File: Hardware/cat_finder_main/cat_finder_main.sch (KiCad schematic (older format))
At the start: 28 parts, among them J1 BATT, J10 Analog, J2 BME280, J3 CSS811, J4 DRIVERS, J5 GY-87, J7 FTDI, J8 Digital, J9 i2c, SW1 SW_DIP_x02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

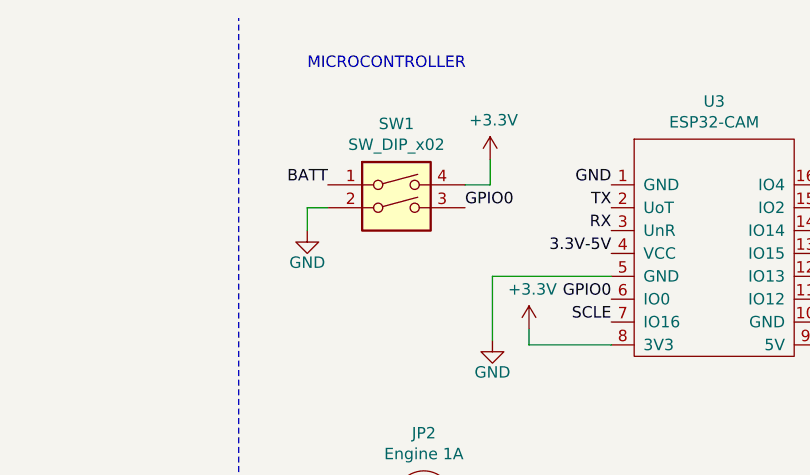
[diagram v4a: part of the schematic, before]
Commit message: change prog pines delete switch
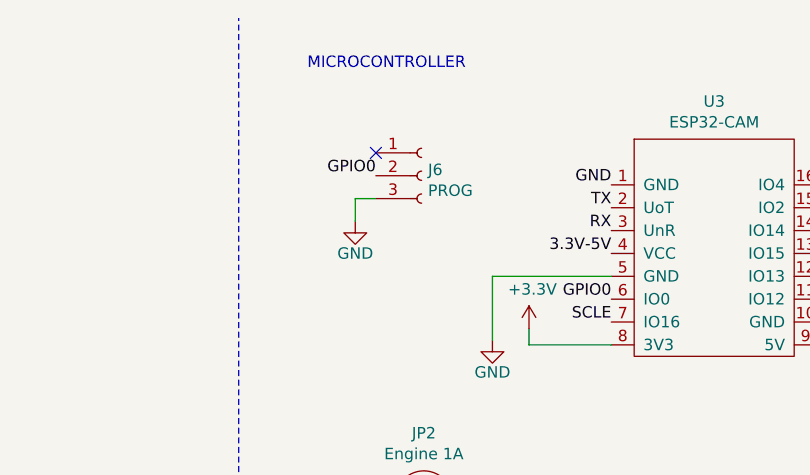
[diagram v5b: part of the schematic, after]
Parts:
- removed SW1: SW_DIP_x02, connectors:DP-02, symbol Switch:SW_DIP_x02
- added J6: PROG, Connector_PinHeader_2.54mm:PinHeader_1x03_P2.54mm_Vertical, symbol Connector:Conn_01x03_Female
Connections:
- net GND: now also J6.3 (Pin_3)
- net GPIO0: now also J6.2 (Pin_2)
- no-connect marks 4 -> 5
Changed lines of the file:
@@
 L power:GND #PWR023
 U 1 1 5D494473
-P 7300 1400
-F 0 "#PWR023" H 7300 1150 50  0001 C CNN
-F 1 "GND" H 7300 1260 50  0000 C CNN
-F 2 "" H 7300 1400 50  0001 C CNN
-F 3 "" H 7300 1400 50  0001 C CNN
-	1    7300 1400
-	1    0    0    -1
-$EndComp
-Text Label 7990 1300 0    50   ~ 0
+P 7510 1360
+F 0 "#PWR023" H 7510 1110 50  0001 C CNN
+F 1 "GND" H 7510 1220 50  0000 C CNN
+F 2 "" H 7510 1360 50  0001 C CNN
+F 3 "" H 7510 1360 50  0001 C CNN
+	1    7510 1360
+	1    0    0    -1
+$EndComp
+Text Label 7600 1160 2    50   ~ 0
 GPIO0
 Wire Notes Line
@@
 	1    0    0    -1
 $EndComp
+Wire Wire Line
+	7510 1360 7510 1260
+Wire Wire Line
+	7510 1260 7600 1260
+$Comp
+L power:+3.3V #PWR09
+U 1 1 5D739360
+P 4400 1180
+F 0 "#PWR09" H 4400 1030 50  0001 C CNN
+F 1 "+3.3V" H 4415 1353 50  0000 C CNN
+F 2 "" H 4400 1180 50  0001 C CNN
+F 3 "" H 4400 1180 50  0001 C CNN
+	1    4400 1180
+	1    0    0    -1
+$EndComp
+Wire Wire Line
+	4400 1180 4400 1400
+$Comp
+L Connector:Conn_01x03_Female J6
+U 1 1 5D721C40
+P 7800 1160
+F 0 "J6" H 7828 1186 50  0000 L CNN
+F 1 "PROG" H 7828 1095 50  0000 L CNN
+F 2 "Connector_PinHeader_2.54mm:PinHeader_1x03_P2.54mm_Vertical" H 7800 1160 50  0001 C CNN
+F 3 "~" H 7800 1160 50  0001 C CNN
+	1    7800 1160
+	1    0    0    -1
+$EndComp
+NoConn ~ 7600 1060
 $Comp
 L electroniccats:ESP32-CAM U3
@@
 	1    0    0    -1
 $EndComp
-$Comp
-L Switch:SW_DIP_x02 SW1
-U 1 1 5D6FB55A
-P 7690 1300
-F 0 "SW1" H 7690 1667 50  0000 C CNN
-F 1 "SW_DIP_x02" H 7690 1576 50  0000 C CNN
-F 2 "connectors:DP-02" H 7690 1300 50  0001 C CNN
-F 3 "~" H 7690 1300 50  0001 C CNN
-	1    7690 1300
-	1    0    0    -1
-$EndComp
-Wire Wire Line
-	7300 1400 7300 1300
-Wire Wire Line
-	7300 1300 7390 1300
-Text Label 7390 1200 2    50   ~ 0
-BATT
-$Comp
-L power:+3.3V #PWR?
-U 1 1 5D736D41
-P 8100 1090
-F 0 "#PWR?" H 8100 940 50  0001 C CNN
-F 1 "+3.3V" H 8115 1263 50  0000 C CNN
-F 2 "" H 8100 1090 50  0001 C CNN
-F 3 "" H 8100 1090 50  0001 C CNN
-	1    8100 1090
-	1    0    0    -1
-$EndComp
-Wire Wire Line
-	7990 1200 8100 1200
-Wire Wire Line
-	8100 1200 8100 1090
-$Comp
-L power:+3.3V #PWR?
-U 1 1 5D739360
-P 4400 1180
-F 0 "#PWR?" H 4400 1030 50  0001 C CNN
-F 1 "+3.3V" H 4415 1353 50  0000 C CNN
-F 2 "" H 4400 1180 50  0001 C CNN
-F 3 "" H 4400 1180 50  0001 C CNN
-	1    4400 1180
-	1    0    0    -1
-$EndComp
-Wire Wire Line
-	4400 1180 4400 1400
 $EndSCHEMATC

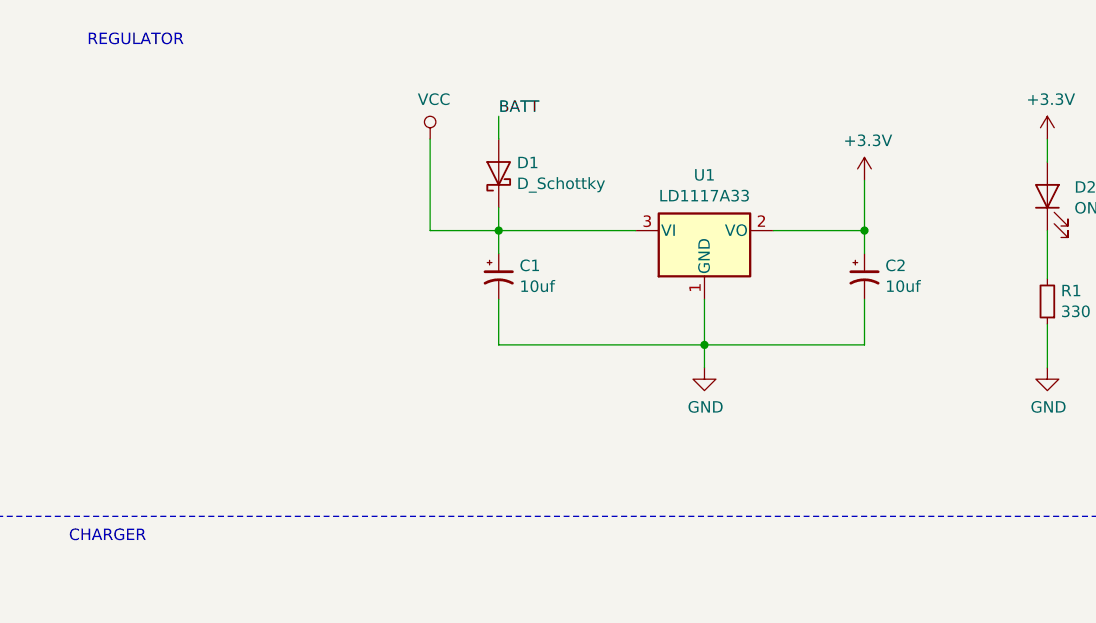
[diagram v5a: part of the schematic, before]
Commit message: add swich on/off
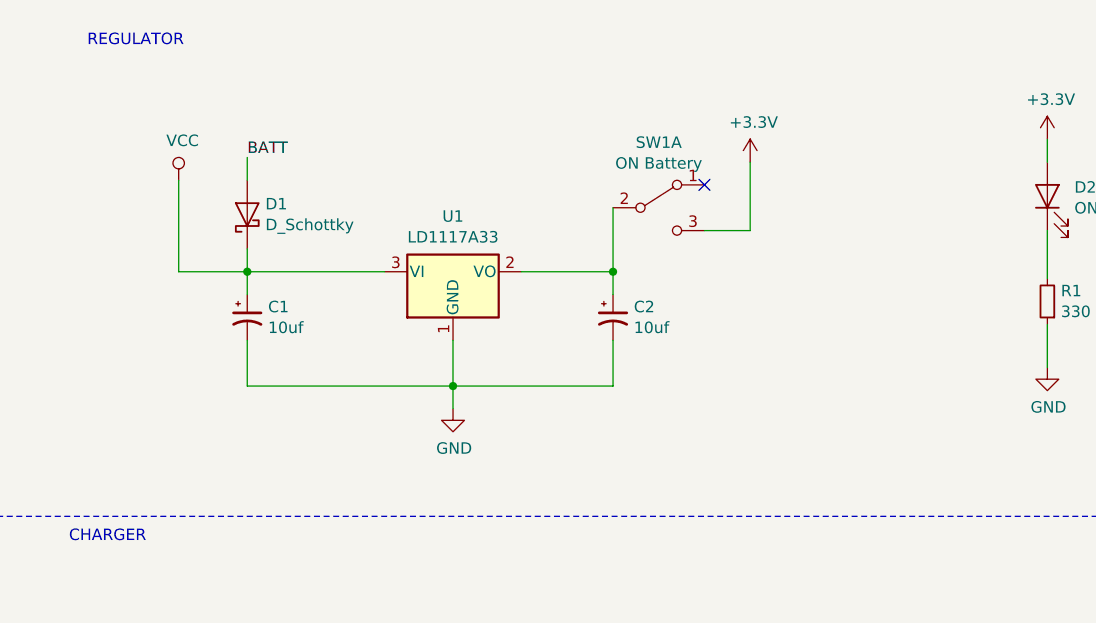
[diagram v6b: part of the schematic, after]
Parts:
- added SW1: ON Battery, connectors:SW_1825116-1, symbol Switch:SW_DPDT_x2
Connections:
- net +3V3: now also SW1.3 (C); no longer C2.1, U1.2 (VO)
- new net: C2.1, SW1.2 (B), U1.2 (VO)
- no-connect marks 5 -> 6
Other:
- moved on the sheet: C1, C2, D1, U1
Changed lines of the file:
@@
 L Device:D_Schottky D1
 U 1 1 5D1FB64C
-P 2800 1150
-F 0 "D1" V 2846 1071 50  0000 R CNN
-F 1 "D_Schottky" V 2755 1071 50  0000 R CNN
-F 2 "Diode_THT:D_A-405_P10.16mm_Horizontal" H 2800 1150 50  0001 C CNN
-F 3 "https://www.mouser.mx/datasheet/2/427/sb220-104141.pdf" H 2800 1150 50  0001 C CNN
-F 4 "SB260-E3/54" V 2800 1150 50  0001 C CNN "manf#"
-	1    2800 1150
+P 1700 1330
+F 0 "D1" V 1746 1251 50  0000 R CNN
+F 1 "D_Schottky" V 1655 1251 50  0000 R CNN
+F 2 "Diode_THT:D_A-405_P10.16mm_Horizontal" H 1700 1330 50  0001 C CNN
+F 3 "https://www.mouser.mx/datasheet/2/427/sb220-104141.pdf" H 1700 1330 50  0001 C CNN
+F 4 "SB260-E3/54" V 1700 1330 50  0001 C CNN "manf#"
+	1    1700 1330
 	0    -1   -1   0
 $EndComp
@@
 L power:GND #PWR07
 U 1 1 5D244C67
-P 3700 2000
-F 0 "#PWR07" H 3700 1750 50  0001 C CNN
-F 1 "GND" H 3705 1827 50  0000 C CNN
-F 2 "" H 3700 2000 50  0001 C CNN
-F 3 "" H 3700 2000 50  0001 C CNN
-	1    3700 2000
+P 2600 2180
+F 0 "#PWR07" H 2600 1930 50  0001 C CNN
+F 1 "GND" H 2605 2007 50  0000 C CNN
+F 2 "" H 2600 2180 50  0001 C CNN
+F 3 "" H 2600 2180 50  0001 C CNN
+	1    2600 2180
 	1    0    0    -1
 $EndComp
@@
 L Regulator_Linear:LD1117S12TR_SOT223 U1
 U 1 1 5D24562A
-P 3700 1400
-F 0 "U1" H 3700 1642 50  0000 C CNN
-F 1 "LD1117A33" H 3700 1551 50  0000 C CNN
-F 2 "Package_TO_SOT_THT:TO-220-3_Vertical" H 3700 1600 50  0001 C CNN
-F 3 "https://www.mouser.mx/datasheet/2/389/ld1117a-974076.pdf" H 3800 1150 50  0001 C CNN
-F 4 "LD1117AV33" H 3700 1400 50  0001 C CNN "manf#"
-	1    3700 1400
-	1    0    0    -1
-$EndComp
-Wire Wire Line
-	3700 1900 3700 1700
-Connection ~ 3700 1900
-Wire Wire Line
-	3700 2000 3700 1900
+P 2600 1580
+F 0 "U1" H 2600 1822 50  0000 C CNN
+F 1 "LD1117A33" H 2600 1731 50  0000 C CNN
+F 2 "Package_TO_SOT_THT:TO-220-3_Vertical" H 2600 1780 50  0001 C CNN
+F 3 "https://www.mouser.mx/datasheet/2/389/ld1117a-974076.pdf" H 2700 1330 50  0001 C CNN
+F 4 "LD1117AV33" H 2600 1580 50  0001 C CNN "manf#"
+	1    2600 1580
+	1    0    0    -1
+$EndComp
+Wire Wire Line
+	2600 2080 2600 1880
+Connection ~ 2600 2080
+Wire Wire Line
+	2600 2180 2600 2080
 $Comp
 L power:VCC #PWR017
@@
 $EndComp
 Wire Wire Line
-	2800 1700 2800 1900
-Wire Wire Line
-	2800 1900 3700 1900
-Wire Wire Line
-	2800 1300 2800 1400
-Wire Wire Line
-	3400 1400 2800 1400
-Connection ~ 2800 1400
-Wire Wire Line
-	2800 1400 2800 1500
+	1700 1880 1700 2080
+Wire Wire Line
+	1700 2080 2600 2080
+Wire Wire Line
+	1700 1480 1700 1580
+Wire Wire Line
+	2300 1580 1700 1580
+Connection ~ 1700 1580
+Wire Wire Line
+	1700 1580 1700 1680
 $Comp
 L power:VCC #PWR04
 U 1 1 5D24A1C2
-P 2500 1000
-F 0 "#PWR04" H 2500 850 50  0001 C CNN
-F 1 "VCC" H 2517 1173 50  0000 C CNN
-F 2 "" H 2500 1000 50  0001 C CNN
-F 3 "" H 2500 1000 50  0001 C CNN
-	1    2500 1000
-	1    0    0    -1
-$EndComp
-Wire Wire Line
-	2800 900  2800 1000
-Wire Wire Line
-	4400 1700 4400 1900
-Wire Wire Line
-	4400 1900 3700 1900
-Wire Wire Line
-	4000 1400 4400 1400
-Wire Wire Line
-	4400 1400 4400 1500
-Connection ~ 4400 1400
+P 1400 1180
+F 0 "#PWR04" H 1400 1030 50  0001 C CNN
+F 1 "VCC" H 1417 1353 50  0000 C CNN
+F 2 "" H 1400 1180 50  0001 C CNN
+F 3 "" H 1400 1180 50  0001 C CNN
+	1    1400 1180
+	1    0    0    -1
+$EndComp
+Wire Wire Line
+	1700 1080 1700 1180
+Wire Wire Line
+	3300 1880 3300 2080
+Wire Wire Line
+	3300 2080 2600 2080
+Wire Wire Line
+	2900 1580 3300 1580
+Wire Wire Line
+	3300 1580 3300 1680
+Connection ~ 3300 1580
 $Comp
 L power:+3.3V #PWR012
@@
 L Device:CP1_Small C1
 U 1 1 5D35F3A4
-P 2800 1600
-F 0 "C1" H 2891 1646 50  0000 L CNN
-F 1 "10uf" H 2891 1555 50  0000 L CNN
-F 2 "Capacitor_THT:CP_Radial_D5.0mm_P2.00mm" H 2800 1600 50  0001 C CNN
-F 3 "https://www.mouser.mx/datasheet/2/445/860010372001-1093821.pdf" H 2800 1600 50  0001 C CNN
-F 4 "860010372001" H 2800 1600 50  0001 C CNN "manf#"
-	1    2800 1600
+P 1700 1780
+F 0 "C1" H 1791 1826 50  0000 L CNN
+F 1 "10uf" H 1791 1735 50  0000 L CNN
+F 2 "Capacitor_THT:CP_Radial_D5.0mm_P2.00mm" H 1700 1780 50  0001 C CNN
+F 3 "https://www.mouser.mx/datasheet/2/445/860010372001-1093821.pdf" H 1700 1780 50  0001 C CNN
+F 4 "860010372001" H 1700 1780 50  0001 C CNN "manf#"
+	1    1700 1780
 	1    0    0    -1
 $EndComp
@@
 L Device:CP1_Small C2
 U 1 1 5D36122D
-P 4400 1600
-F 0 "C2" H 4491 1646 50  0000 L CNN
-F 1 "10uf" H 4491 1555 50  0000 L CNN
-F 2 "Capacitor_THT:CP_Radial_D5.0mm_P2.00mm" H 4400 1600 50  0001 C CNN
-F 3 "https://www.mouser.mx/datasheet/2/445/860010372001-1093821.pdf" H 4400 1600 50  0001 C CNN
-F 4 "860010372001" H 4400 1600 50  0001 C CNN "manf#"
-	1    4400 1600
+P 3300 1780
+F 0 "C2" H 3391 1826 50  0000 L CNN
+F 1 "10uf" H 3391 1735 50  0000 L CNN
+F 2 "Capacitor_THT:CP_Radial_D5.0mm_P2.00mm" H 3300 1780 50  0001 C CNN
+F 3 "https://www.mouser.mx/datasheet/2/445/860010372001-1093821.pdf" H 3300 1780 50  0001 C CNN
+F 4 "860010372001" H 3300 1780 50  0001 C CNN "manf#"
+	1    3300 1780
 	1    0    0    -1
 $EndComp
@@
 Text Label 9180 2990 2    50   ~ 0
 GPIO13
-Text Label 2800 900  0    50   ~ 0
+Text Label 1700 1080 0    50   ~ 0
 BATT
 Wire Wire Line
-	2500 1000 2500 1400
-Wire Wire Line
-	2500 1400 2800 1400
+	1400 1180 1400 1580
+Wire Wire Line
+	1400 1580 1700 1580
 Wire Wire Line
 	3580 3500 3580 3690
@@
 L power:+3.3V #PWR09
 U 1 1 5D739360
-P 4400 1180
-F 0 "#PWR09" H 4400 1030 50  0001 C CNN
-F 1 "+3.3V" H 4415 1353 50  0000 C CNN
-F 2 "" H 4400 1180 50  0001 C CNN
-F 3 "" H 4400 1180 50  0001 C CNN
-	1    4400 1180
-	1    0    0    -1
-$EndComp
-Wire Wire Line
-	4400 1180 4400 1400
+P 3900 1100
+F 0 "#PWR09" H 3900 950 50  0001 C CNN
+F 1 "+3.3V" H 3915 1273 50  0000 C CNN
+F 2 "" H 3900 1100 50  0001 C CNN
+F 3 "" H 3900 1100 50  0001 C CNN
+	1    3900 1100
+	1    0    0    -1
+$EndComp
 $Comp
 L Connector:Conn_01x03_Female J6
@@
 	1    0    0    -1
 $EndComp
+$Comp
+L Switch:SW_DPDT_x2 SW1
+U 1 1 5D7346B1
+P 3500 1300
+F 0 "SW1" H 3500 1585 50  0000 C CNN
+F 1 "ON Battery" H 3500 1494 50  0000 C CNN
+F 2 "connectors:SW_1825116-1" H 3500 1300 50  0001 C CNN
+F 3 "~" H 3500 1300 50  0001 C CNN
+	1    3500 1300
+	1    0    0    -1
+$EndComp
+Wire Wire Line
+	3300 1300 3300 1580
+Wire Wire Line
+	3700 1400 3900 1400
+Wire Wire Line
+	3900 1400 3900 1100
+NoConn ~ 3700 1200
 $EndSCHEMATC

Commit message: add pin bast
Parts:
- added J11: Bast Pin, Connector_PinSocket_2.54mm:PinSocket_1x05_P2.54mm_Vertical, symbol Connector:Conn_01x05_Female
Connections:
- net 10: now also J11.1 (Pin_1)
- net 11: now also J11.2 (Pin_2); no longer JP8.1
- net 12: now also J11.3 (Pin_3)
- net 13: now also J11.4 (Pin_4)
- net A0: now also J11.5 (Pin_5)
- net A1: now also JP8.1; no longer JP7.1
- net A2: now also JP7.1
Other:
- moved on the sheet: JP10, JP7, JP8, JP9
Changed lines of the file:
@@
 Text Label 8550 6050 3    50   ~ 0
 SCL
-Text Label 10150 5500 2    50   ~ 0
+Text Label 10130 4830 2    50   ~ 0
 A3
-Text Label 10750 5210 0    50   ~ 0
+Text Label 10730 4540 0    50   ~ 0
 GPIO12
-Text Label 10750 4900 0    50   ~ 0
+Text Label 10730 4230 0    50   ~ 0
 GPIO13
-Text Label 10750 5500 0    50   ~ 0
+Text Label 10730 4830 0    50   ~ 0
 GPIO15
-Text Label 10700 5800 0    50   ~ 0
+Text Label 10680 5130 0    50   ~ 0
 GPIO14
 $Comp
@@
 Text Label 5290 6000 2    50   ~ 0
 VCC-IN
-Text Label 10150 5210 2    50   ~ 0
+Text Label 10300 5600 2    50   ~ 0
 11
-Text Label 10150 4900 2    50   ~ 0
+Text Label 10130 4540 2    50   ~ 0
 A1
-Text Label 10140 5800 2    50   ~ 0
+Text Label 10120 5130 2    50   ~ 0
 9
 $Comp
@@
 L Device:Jumper_NO_Small JP7
 U 1 1 5D4CD611
-P 10470 4900
-F 0 "JP7" H 10470 5085 50  0000 C CNN
-F 1 "Engine 1 A" H 10470 4994 50  0000 C CNN
-F 2 "Jumper:SolderJumper-2_P1.3mm_Open_RoundedPad1.0x1.5mm" H 10470 4900 50  0001 C CNN
-F 3 "~" H 10470 4900 50  0001 C CNN
-	1    10470 4900
-	1    0    0    -1
-$EndComp
-Wire Wire Line
-	10570 4900 10750 4900
-Wire Wire Line
-	10370 4900 10150 4900
+P 10450 4230
+F 0 "JP7" H 10450 4415 50  0000 C CNN
+F 1 "Engine 1 A" H 10450 4324 50  0000 C CNN
+F 2 "Jumper:SolderJumper-2_P1.3mm_Open_RoundedPad1.0x1.5mm" H 10450 4230 50  0001 C CNN
+F 3 "~" H 10450 4230 50  0001 C CNN
+	1    10450 4230
+	1    0    0    -1
+$EndComp
+Wire Wire Line
+	10550 4230 10730 4230
+Wire Wire Line
+	10350 4230 10130 4230
 $Comp
 L Device:Jumper_NO_Small JP8
 U 1 1 5D4D2033
-P 10480 5210
-F 0 "JP8" H 10480 5395 50  0000 C CNN
-F 1 "Engine 1B" H 10480 5304 50  0000 C CNN
-F 2 "Jumper:SolderJumper-2_P1.3mm_Open_RoundedPad1.0x1.5mm" H 10480 5210 50  0001 C CNN
-F 3 "~" H 10480 5210 50  0001 C CNN
-	1    10480 5210
-	1    0    0    -1
-$EndComp
-Wire Wire Line
-	10580 5210 10750 5210
-Wire Wire Line
-	10380 5210 10150 5210
+P 10460 4540
+F 0 "JP8" H 10460 4725 50  0000 C CNN
+F 1 "Engine 1B" H 10460 4634 50  0000 C CNN
+F 2 "Jumper:SolderJumper-2_P1.3mm_Open_RoundedPad1.0x1.5mm" H 10460 4540 50  0001 C CNN
+F 3 "~" H 10460 4540 50  0001 C CNN
+	1    10460 4540
+	1    0    0    -1
+$EndComp
+Wire Wire Line
+	10560 4540 10730 4540
+Wire Wire Line
+	10360 4540 10130 4540
 $Comp
 L Device:Jumper_NO_Small JP9
 U 1 1 5D4D5761
-P 10450 5500
-F 0 "JP9" H 10450 5685 50  0000 C CNN
-F 1 "Engine 2A" H 10450 5594 50  0000 C CNN
-F 2 "Jumper:SolderJumper-2_P1.3mm_Open_RoundedPad1.0x1.5mm" H 10450 5500 50  0001 C CNN
-F 3 "~" H 10450 5500 50  0001 C CNN
-	1    10450 5500
-	1    0    0    -1
-$EndComp
-Wire Wire Line
-	10550 5500 10750 5500
-Wire Wire Line
-	10150 5500 10350 5500
+P 10430 4830
+F 0 "JP9" H 10430 5015 50  0000 C CNN
+F 1 "Engine 2A" H 10430 4924 50  0000 C CNN
+F 2 "Jumper:SolderJumper-2_P1.3mm_Open_RoundedPad1.0x1.5mm" H 10430 4830 50  0001 C CNN
+F 3 "~" H 10430 4830 50  0001 C CNN
+	1    10430 4830
+	1    0    0    -1
+$EndComp
+Wire Wire Line
+	10530 4830 10730 4830
+Wire Wire Line
+	10130 4830 10330 4830
 $Comp
 L Device:Jumper_NO_Small JP10
 U 1 1 5D4DA54D
-P 10420 5800
-F 0 "JP10" H 10420 5985 50  0000 C CNN
-F 1 "Engine 2B" H 10420 5894 50  0000 C CNN
-F 2 "Jumper:SolderJumper-2_P1.3mm_Open_RoundedPad1.0x1.5mm" H 10420 5800 50  0001 C CNN
-F 3 "~" H 10420 5800 50  0001 C CNN
-	1    10420 5800
-	1    0    0    -1
-$EndComp
-Wire Wire Line
-	10520 5800 10700 5800
-Wire Wire Line
-	10320 5800 10140 5800
+P 10400 5130
+F 0 "JP10" H 10400 5315 50  0000 C CNN
+F 1 "Engine 2B" H 10400 5224 50  0000 C CNN
+F 2 "Jumper:SolderJumper-2_P1.3mm_Open_RoundedPad1.0x1.5mm" H 10400 5130 50  0001 C CNN
+F 3 "~" H 10400 5130 50  0001 C CNN
+	1    10400 5130
+	1    0    0    -1
+$EndComp
+Wire Wire Line
+	10500 5130 10680 5130
+Wire Wire Line
+	10300 5130 10120 5130
 $Comp
 L power:+3.3V #PWR0101
@@
 	3900 1400 3900 1100
 NoConn ~ 3700 1200
+Text Label 10130 4230 2    50   ~ 0
+A2
+$Comp
+L Connector:Conn_01x05_Female J11
+U 1 1 5D7B90BA
+P 10500 5700
+F 0 "J11" H 10528 5726 50  0000 L CNN
+F 1 "Bast Pin" H 10528 5635 50  0000 L CNN
+F 2 "Connector_PinSocket_2.54mm:PinSocket_1x05_P2.54mm_Vertical" H 10500 5700 50  0001 C CNN
+F 3 "~" H 10500 5700 50  0001 C CNN
+	1    10500 5700
+	1    0    0    -1
+$EndComp
+Text Label 10300 5500 2    50   ~ 0
+10
+Text Label 10300 5700 2    50   ~ 0
+12
+Text Label 10300 5800 2    50   ~ 0
+13
+Text Label 10300 5900 2    50   ~ 0
+A0
 $EndSCHEMATC

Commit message: move tracks
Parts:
- added D4: D_Schottky, Diode_THT:D_DO-41_SOD81_P10.16mm_Horizontal, symbol Device:D_Schottky
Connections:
- net VCC: now also D4.2 (A); no longer C1.1, D1.1 (K), J7.4 (Pin_4), U1.3 (VI)
- new net: C1.1, D1.1 (K), D4.1 (K), U1.3 (VI)
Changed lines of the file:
@@
 EESchema Schematic File Version 4
+LIBS:cat_finder_main-cache
 EELAYER 29 0
 EELAYER END
@@
 $EndComp
 Wire Wire Line
-	10230 2870 10230 2970
-Wire Wire Line
-	10230 2970 10530 2970
-Wire Wire Line
 	10230 3270 10230 3170
 Wire Wire Line
@@
 Wire Wire Line
 	2600 2180 2600 2080
-$Comp
-L power:VCC #PWR017
-U 1 1 5D247292
-P 10230 2870
-F 0 "#PWR017" H 10230 2720 50  0001 C CNN
-F 1 "VCC" H 10247 3043 50  0000 C CNN
-F 2 "" H 10230 2870 50  0001 C CNN
-F 3 "" H 10230 2870 50  0001 C CNN
-	1    10230 2870
-	1    0    0    -1
-$EndComp
 Wire Wire Line
 	1700 1880 1700 2080
@@
 Wire Wire Line
 	5200 1810 5200 2000
-NoConn ~ 12410 3690
+NoConn ~ 10530 2970
 Text Label 2740 3860 0    50   ~ 0
 BATT
@@
 Text Label 1700 1080 0    50   ~ 0
 BATT
-Wire Wire Line
-	1400 1180 1400 1580
 Wire Wire Line
 	1400 1580 1700 1580
@@
 Text Label 10300 5900 2    50   ~ 0
 A0
+$Comp
+L Device:D_Schottky D4
+U 1 1 5D782221
+P 1400 1330
+F 0 "D4" V 1450 1670 50  0000 R CNN
+F 1 "D_Schottky" V 1350 1830 50  0000 R CNN
+F 2 "Diode_THT:D_DO-41_SOD81_P10.16mm_Horizontal" H 1400 1330 50  0001 C CNN
+F 3 "mouser.mx/datasheet/2/345/1n5817-1n5819-24580.pdf" H 1400 1330 50  0001 C CNN
+F 4 "1N5817-T" V 1400 1330 50  0001 C CNN "manf#"
+	1    1400 1330
+	0    -1   -1   0
+$EndComp
+Wire Wire Line
+	1400 1480 1400 1580
 $EndSCHEMATC
